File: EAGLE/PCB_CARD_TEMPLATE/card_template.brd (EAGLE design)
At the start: 24 x 60 mm, 0 parts

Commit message: have footprints complete
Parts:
- added M1: MOUNTING_3M_3.2MM, ENERTECH_MISC:MOUNTING_3M_3.2MM
- added X1: CONN_SMD_67P-P0.5-V_NASB0-S6701-TS50, ENERTECH_MISC:CONN_SMD_67P-P0.5-V_NASB0-S6701-TS50
- added X2: M.2_MKEY_FINGERS, ENERTECH_MISC:M.2_MKEY_FINGERS

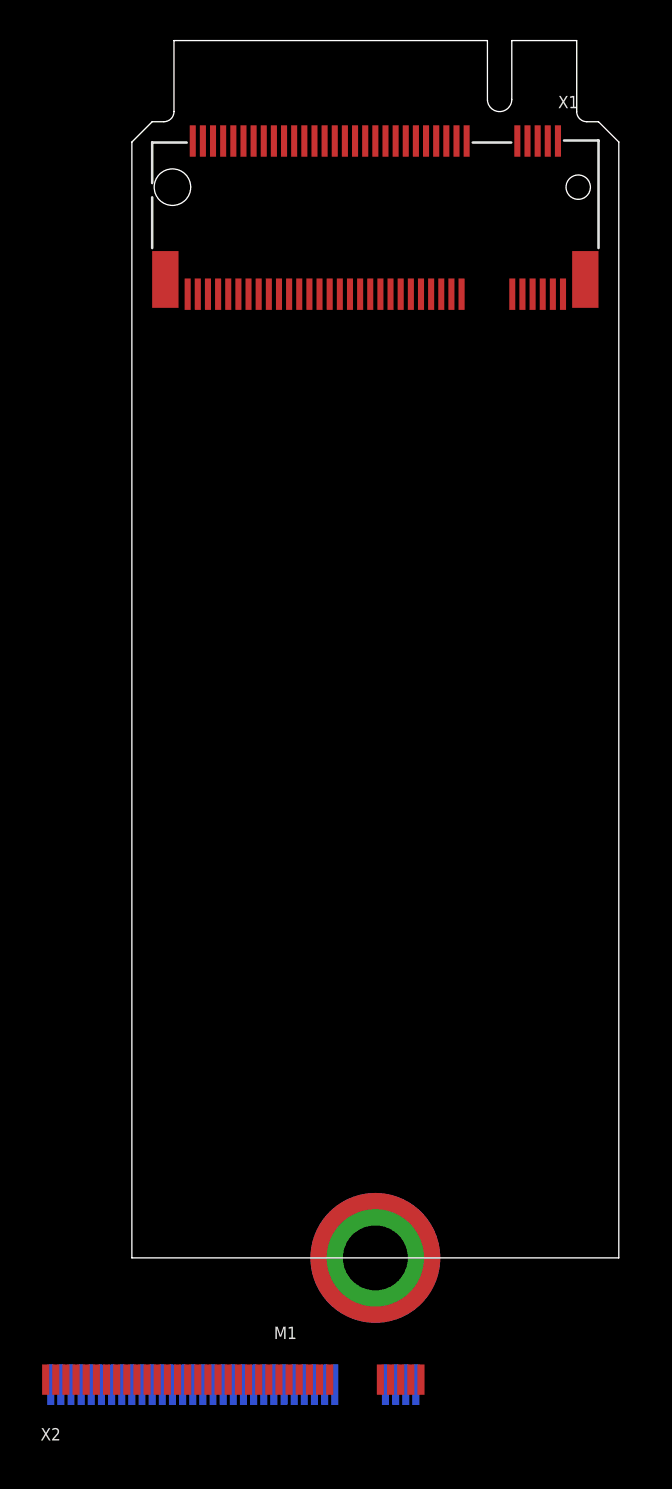
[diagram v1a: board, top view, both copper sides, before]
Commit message: completed accessory card template
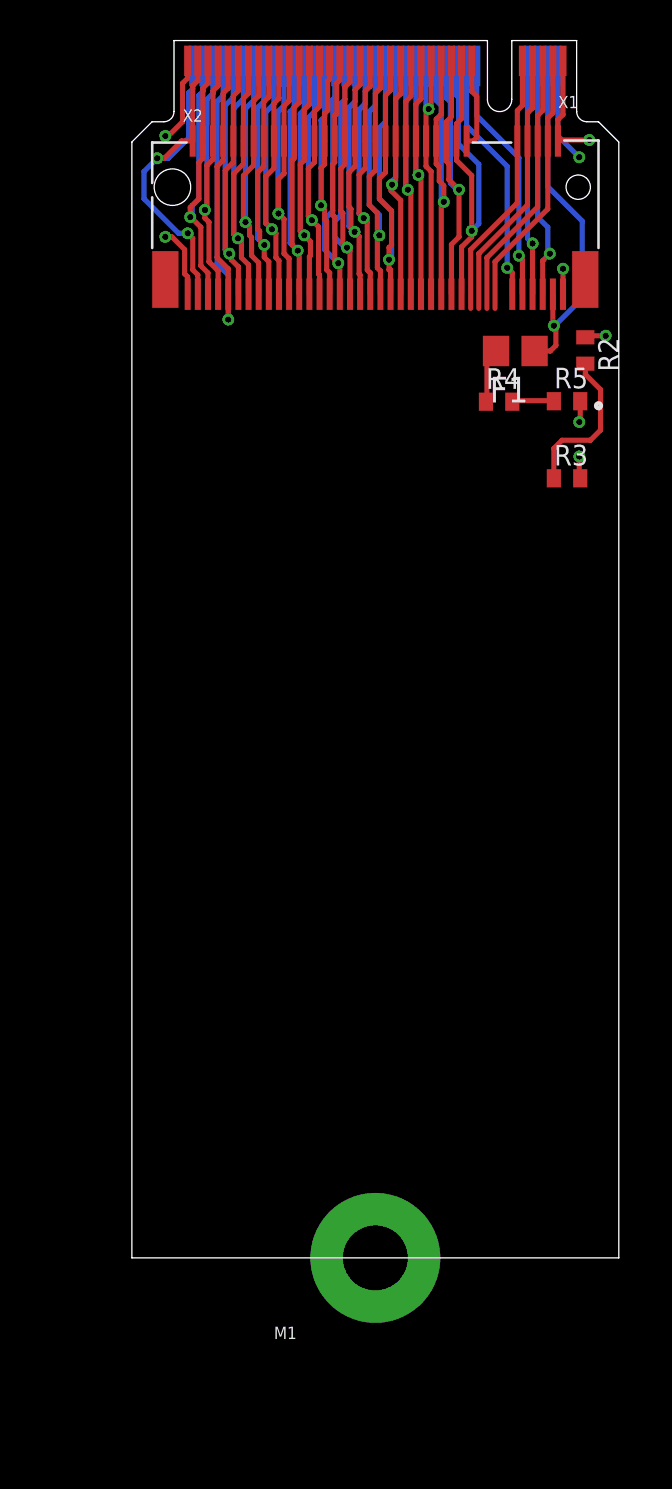
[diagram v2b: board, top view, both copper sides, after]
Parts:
- added F1: 100mA, _NIBE_rcl:R0805
- added R2, R4: 470R, _NIBE_rcl:R0603
- added R3, R5: LED_GREEN, _NIBE_rcl:R0603
- moved X2 65.4 mm to (12.0, 60.0)
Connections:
- new net +3V3: R2.1, X1.P$1, X2.74
- new net +5V: F1.2, R4.1
- new net GND: R3.2, R5.2, X1.P$2, X1.P$75, X2.1, X2.75
- new net N$1: X1.P$23, X1.P$24, X2.52, X2.53
- new net N$10: X1.P$59, X1.P$60, X2.16, X2.17
- new net N$11: X1.P$57, X1.P$58, X2.18, X2.19
- new net N$12: X1.P$55, X1.P$56, X2.20, X2.21
- new net N$13: X1.P$53, X1.P$54, X2.22, X2.23
- new net N$14: X1.P$51, X1.P$52, X2.24, X2.25
- new net N$15: X1.P$21, X1.P$22, X2.54, X2.55
- new net N$16: X1.P$27, X1.P$28, X2.48, X2.49
- new net N$17: X1.P$29, X1.P$30, X2.46, X2.47
- new net N$18: X1.P$31, X1.P$32, X2.44, X2.45
- new net N$19: X1.P$33, X1.P$34, X2.42, X2.43
- new net N$2: X1.P$25, X1.P$26, X2.50, X2.51
- new net N$20: X1.P$35, X1.P$36, X2.40, X2.41
- new net N$21: X1.P$37, X1.P$38, X2.38, X2.39
- new net N$22: X1.P$39, X1.P$40, X2.36, X2.37
- new net N$23: X1.P$41, X1.P$42, X2.34, X2.35
- new net N$24: X1.P$43, X1.P$44, X2.32, X2.33
- new net N$25: X1.P$45, X1.P$46, X2.30, X2.31
- new net N$26: X1.P$47, X1.P$48, X2.28, X2.29
- new net N$27: X1.P$49, X1.P$50, X2.26, X2.27
- new net N$28: X1.P$11, X2.56
- new net N$29: X1.P$9, X2.58
- new net N$3: X1.P$73, X1.P$74, X2.2, X2.3
- new net N$30: X1.P$7, X2.68
- new net N$31: X1.P$5, X2.70
- new net N$32: F1.1, X1.P$3, X2.72
- new net N$33: R2.2, R3.1
- new net N$35: X1.P$4, X2.73
- new net N$36: X1.P$6, X2.71
- new net N$37: X1.P$8, X2.69
- new net N$38: X1.P$10, X2.67
- new net N$39: X1.P$20, X2.57
- new net N$4: X1.P$71, X1.P$72, X2.4, X2.5
- new net N$40: R4.2, R5.1
- new net N$5: X1.P$69, X1.P$70, X2.6, X2.7
- new net N$6: X1.P$67, X1.P$68, X2.8, X2.9
- new net N$7: X1.P$65, X1.P$66, X2.10, X2.11
- new net N$8: X1.P$63, X1.P$64, X2.12, X2.13
- new net N$9: X1.P$61, X1.P$62, X2.14, X2.15
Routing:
- net N$6: track 0.00 -> 26.1 mm, vias 0 -> 1
- net N$20: track 0.00 -> 22.1 mm, vias 0 -> 1
- net N$25: track 0.00 -> 22.0 mm, vias 0 -> 1
- net N$7: track 0.00 -> 21.5 mm, vias 0 -> 1
- net N$24: track 0.00 -> 21.3 mm, vias 0 -> 1
- net N$13: track 0.00 -> 21.1 mm, vias 0 -> 1
- net N$10: track 0.00 -> 21.0 mm, vias 0 -> 1
- net N$8: track 0.00 -> 20.9 mm, vias 0 -> 1
- net N$15: track 0.00 -> 20.8 mm, vias 0 -> 1
- net N$21: track 0.00 -> 20.7 mm, vias 0 -> 1
- net N$14: track 0.00 -> 20.4 mm, vias 0 -> 1
- net N$11: track 0.00 -> 20.4 mm, vias 0 -> 1
- net N$23: track 0.00 -> 20.4 mm, vias 0 -> 1
- net N$3: track 0.00 -> 20.1 mm, vias 0 -> 2
- net N$9: track 0.00 -> 20.0 mm, vias 0 -> 1
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- added copper zone on layer 2, net +3V3
- added copper zone on layer 15, net GND

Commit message: pic24 card is done, gerbers and jlc files generated
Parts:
- removed F1: 100mA, _NIBE_rcl:R0805
- removed R4: 470R, _NIBE_rcl:R0603
- removed R5: LED_GREEN, _NIBE_rcl:R0603
- moved R3 3.00 mm to (21.4, 41.4)
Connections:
- removed net N$32: F1.1, X1.P$3, X2.72
- removed net N$35: X1.P$4, X2.73
- removed net N$40: R4.2, R5.1
- net +5V: now also X1.P$3, X2.72; no longer F1.2, R4.1
- net GND: now also X1.P$4, X2.73; no longer R5.2
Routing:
- net N$32: track 17.9 -> 0.00 mm, vias 1 -> 0
- net N$35: track 13.4 -> 0.00 mm
- net +5V: track 2.71 -> 15.7 mm, vias 0 -> 1
- net GND: track 15.5 -> 8.77 mm, vias 5 -> 4
- net N$33: track 7.73 -> 3.70 mm
- net N$40: track 2.11 -> 0.00 mm
- added copper zone on layer 1, net GND
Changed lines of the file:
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@@
 <attribute name="VALUE" x="2.5" y="54.25" locked="yes" size="0.6096" layer="27" font="vector" ratio="14"/>
-</element>
-<element name="F1" library="_NIBE_rcl" package="R0805" value="100mA" x="18.9" y="44.7" smashed="yes" rot="R180">
-<attribute name="NAME" x="19.535" y="43.43" size="1.27" layer="25" rot="R180"/>
-<attribute name="VALUE" x="19.535" y="47.24" size="1.27" layer="27" rot="R180"/>
 </element>
 <element name="R2" library="_NIBE_rcl" package="R0603" value="470R" x="22.35" y="44.725" smashed="yes" rot="R270">
@@
 <attribute name="VALUE" x="20.445" y="45.36" size="1.016" layer="27" rot="R270"/>
 </element>
-<element name="R3" library="_NIBE_rcl" package="R0603" value="LED_GREEN" x="21.45" y="38.425" smashed="yes">
-<attribute name="NAME" x="20.815" y="39.06" size="1.016" layer="25"/>
-<attribute name="VALUE" x="20.815" y="36.52" size="1.016" layer="27"/>
-</element>
-<element name="R4" library="_NIBE_rcl" package="R0603" value="470R" x="18.1" y="42.2" smashed="yes">
-<attribute name="NAME" x="17.465" y="42.835" size="1.016" layer="25"/>
-<attribute name="VALUE" x="17.465" y="40.295" size="1.016" layer="27"/>
-</element>
-<element name="R5" library="_NIBE_rcl" package="R0603" value="LED_GREEN" x="21.45" y="42.225" smashed="yes">
-<attribute name="NAME" x="20.815" y="42.86" size="1.016" layer="25"/>
-<attribute name="VALUE" x="20.815" y="40.32" size="1.016" layer="27"/>
+<element name="R3" library="_NIBE_rcl" package="R0603" value="LED_GREEN" x="21.45" y="41.425" smashed="yes">
+<attribute name="NAME" x="20.815" y="42.06" size="1.016" layer="25"/>
+<attribute name="VALUE" x="20.815" y="39.52" size="1.016" layer="27"/>
 </element>
 </elements>
@@
 <contactref element="X2" pad="75"/>
 <contactref element="R3" pad="2"/>
-<contactref element="R5" pad="2"/>
 <polygon width="0.254" layer="15" thermals="no">
 <vertex x="-1" y="-1"/>
@@
 </polygon>
 <via x="1.65" y="50.325" extent="1-16" drill="0.3"/>
-<via x="22.05" y="39.5" extent="1-16" drill="0.3"/>
-<via x="22.05" y="41.2" extent="1-16" drill="0.3"/>
-<wire x1="22.1" y1="42.225" x2="22.1" y2="41.25" width="0.254" layer="1"/>
-<wire x1="22.1" y1="41.25" x2="22.05" y2="41.2" width="0.254" layer="1"/>
-<wire x1="22.1" y1="38.425" x2="22.05" y2="38.475" width="0.254" layer="1"/>
-<wire x1="22.05" y1="38.475" x2="22.05" y2="39.5" width="0.254" layer="1"/>
-<via x="22.55" y="55.1" extent="1-16" drill="0.3"/>
-<wire x1="21" y1="55.049884375" x2="21.050115625" y2="55.1" width="0.254" layer="1"/>
-<wire x1="21.050115625" y1="55.1" x2="22.55" y2="55.1" width="0.254" layer="1"/>
-<wire x1="21.25" y1="56.35" x2="21.25" y2="59" width="0.254" layer="1"/>
-<wire x1="21" y1="55.049884375" x2="21" y2="56.1" width="0.254" layer="1"/>
-<wire x1="21" y1="56.1" x2="21.25" y2="56.35" width="0.254" layer="1"/>
+<via x="23.15" y="41.4" extent="1-16" drill="0.3"/>
+<wire x1="23.15" y1="41.4" x2="22.125" y2="41.4" width="0.254" layer="1"/>
+<wire x1="22.1" y1="41.425" x2="22.125" y2="41.4" width="0.254" layer="1"/>
+<via x="22.55" y="55.1" extent="1-16" drill="0.35"/>
 <wire x1="2.75" y1="59" x2="2.75" y2="58.15" width="0.254" layer="1"/>
 <wire x1="2.75" y1="58.15" x2="2.5" y2="57.9" width="0.254" layer="1"/>
@@
 <wire x1="2.6" y1="49.7" x2="1.975" y2="50.325" width="0.254" layer="1"/>
 <wire x1="1.975" y1="50.325" x2="1.65" y2="50.325" width="0.254" layer="1"/>
+<contactref element="X1" pad="P$4"/>
+<contactref element="X2" pad="73"/>
+<polygon width="0.1524" layer="1" thermals="no">
+<vertex x="20.3" y="54.2"/>
+<vertex x="20.3" y="55.8"/>
+<vertex x="20.6" y="56.1"/>
+<vertex x="20.6" y="59.8"/>
+<vertex x="21.5" y="59.8"/>
+<vertex x="21.5" y="56.1"/>
+<vertex x="21.9" y="55.7"/>
+<vertex x="23" y="55.7"/>
+<vertex x="23" y="54.6"/>
+<vertex x="21.5" y="54.6"/>
+<vertex x="21.1" y="54.2"/>
+</polygon>
+<wire x1="20.75" y1="59" x2="21.25" y2="59" width="0" layer="19" extent="1-1"/>
+<wire x1="21" y1="55.049884375" x2="21.25" y2="59" width="0" layer="19" extent="1-1"/>
+<wire x1="20.5" y1="55.049884375" x2="21" y2="55.049884375" width="0" layer="19" extent="1-1"/>
+<wire x1="22.55" y1="55.1" x2="21" y2="55.049884375" width="0" layer="19" extent="1-1"/>
+<wire x1="22.125" y1="41.4" x2="21" y2="55.049884375" width="0" layer="19" extent="1-1"/>
+<wire x1="2.75" y1="59" x2="20.75" y2="59" width="0" layer="19" extent="1-1"/>
+<wire x1="1.65" y1="50.325" x2="1.65" y2="55.3" width="0" layer="19" extent="1-1"/>
 </signal>
 <signal name="N$3">
@@
 <wire x1="20.5" y1="50.8" x2="20.5" y2="49.6" width="0.254" layer="16"/>
 </signal>
-<signal name="N$32">
-<contactref element="X1" pad="P$3"/>
-<contactref element="X2" pad="72"/>
-<contactref element="F1" pad="1"/>
-<wire x1="20.8" y1="45.95" x2="20.9" y2="45.85" width="0.254" layer="1"/>
-<wire x1="20.9" y1="45.85" x2="20.9" y2="44.975" width="0.254" layer="1"/>
-<wire x1="20.9" y1="44.975" x2="20.625" y2="44.7" width="0.254" layer="1"/>
-<wire x1="19.85" y1="44.7" x2="20.625" y2="44.7" width="0.254" layer="1"/>
-<wire x1="20.75" y1="47.499971875" x2="20.75" y2="46" width="0.254" layer="1"/>
-<wire x1="20.8" y1="45.95" x2="20.75" y2="46" width="0.254" layer="1"/>
-<via x="20.8" y="45.95" extent="1-16" drill="0.3"/>
-<wire x1="20.5" y1="52.8" x2="22.2" y2="51.1" width="0.254" layer="16"/>
-<wire x1="20.85" y1="45.95" x2="20.8" y2="45.95" width="0.254" layer="16"/>
-<wire x1="22.2" y1="51.1" x2="22.2" y2="47.3" width="0.254" layer="16"/>
-<wire x1="22.2" y1="47.3" x2="20.85" y2="45.95" width="0.254" layer="16"/>
-<wire x1="20.5" y1="52.8" x2="20.5" y2="58.75" width="0.254" layer="16"/>
-</signal>
-<signal name="N$35">
-<contactref element="X1" pad="P$4"/>
-<contactref element="X2" pad="73"/>
-<wire x1="20.75" y1="56.425" x2="20.75" y2="59" width="0.254" layer="1"/>
-<wire x1="20.5" y1="56.175" x2="20.75" y2="56.425" width="0.254" layer="1"/>
-<wire x1="20.5" y1="55.049884375" x2="20.5" y2="56.175" width="0.254" layer="1"/>
-<wire x1="20.5" y1="55.049884375" x2="20.5" y2="51.7" width="0.254" layer="1"/>
-<wire x1="20.5" y1="51.7" x2="17.9" y2="49.1" width="0.254" layer="1"/>
-<wire x1="17.9" y1="49.1" x2="17.9" y2="46.8" width="0.254" layer="1"/>
-</signal>
 <signal name="N$36">
 <contactref element="X1" pad="P$6"/>
@@
 <wire x1="22.35" y1="45.375" x2="22.425" y2="45.45" width="0.254" layer="1"/>
 <wire x1="22.425" y1="45.45" x2="23.35" y2="45.45" width="0.254" layer="1"/>
-<via x="22.05" y="54.25" extent="1-16" drill="0.3"/>
-<wire x1="21" y1="58.75" x2="21" y2="55.3" width="0.254" layer="16"/>
-<wire x1="22.05" y1="54.25" x2="21" y2="55.3" width="0.254" layer="16"/>
+<via x="21.95" y="54.25" extent="1-16" drill="0.35"/>
+<wire x1="21" y1="58.75" x2="21" y2="55.2" width="0.254" layer="16"/>
+<wire x1="21.95" y1="54.25" x2="21" y2="55.2" width="0.254" layer="16"/>
 </signal>
 <signal name="+5V">
-<contactref element="F1" pad="2"/>
-<contactref element="R4" pad="1"/>
-<wire x1="17.5" y1="44.25" x2="17.5" y2="42.25" width="0.254" layer="1"/>
-<wire x1="17.95" y1="44.7" x2="17.5" y2="44.25" width="0.254" layer="1"/>
-<wire x1="17.5" y1="42.25" x2="17.45" y2="42.2" width="0.254" layer="1"/>
+<contactref element="X1" pad="P$3"/>
+<contactref element="X2" pad="72"/>
+<wire x1="20.75" y1="47.499971875" x2="20.75" y2="46" width="0.254" layer="1"/>
+<wire x1="20.8" y1="45.95" x2="20.75" y2="46" width="0.254" layer="1"/>
+<via x="20.8" y="45.95" extent="1-16" drill="0.3"/>
+<wire x1="20.5" y1="52.8" x2="22.2" y2="51.1" width="0.254" layer="16"/>
+<wire x1="20.85" y1="45.95" x2="20.8" y2="45.95" width="0.254" layer="16"/>
+<wire x1="22.2" y1="51.1" x2="22.2" y2="47.3" width="0.254" layer="16"/>
+<wire x1="22.2" y1="47.3" x2="20.85" y2="45.95" width="0.254" layer="16"/>
+<wire x1="20.5" y1="52.8" x2="20.5" y2="58.75" width="0.254" layer="16"/>
 </signal>
 <signal name="N$33">
 <contactref element="R2" pad="2"/>
 <contactref element="R3" pad="1"/>
-<wire x1="20.8" y1="38.425" x2="20.8" y2="39.9" width="0.254" layer="1"/>
-<wire x1="22.35" y1="43.55" x2="22.35" y2="44.075" width="0.254" layer="1"/>
-<wire x1="20.8" y1="39.9" x2="21.2" y2="40.3" width="0.254" layer="1"/>
-<wire x1="21.2" y1="40.3" x2="22.6" y2="40.3" width="0.254" layer="1"/>
-<wire x1="22.6" y1="40.3" x2="23.1" y2="40.8" width="0.254" layer="1"/>
-<wire x1="23.1" y1="40.8" x2="23.1" y2="42.8" width="0.254" layer="1"/>
-<wire x1="23.1" y1="42.8" x2="22.35" y2="43.55" width="0.254" layer="1"/>
-</signal>
-<signal name="N$40">
-<contactref element="R5" pad="1"/>
-<contactref element="R4" pad="2"/>
-<wire x1="20.75" y1="42.25" x2="18.75" y2="42.25" width="0.254" layer="1"/>
-<wire x1="18.75" y1="42.25" x2="18.75" y2="42.2" width="0.254" layer="1"/>
-<wire x1="20.75" y1="42.25" x2="20.8" y2="42.225" width="0.254" layer="1"/>
+<wire x1="22.35" y1="44.075" x2="22.35" y2="43.25" width="0.254" layer="1"/>
+<wire x1="21.9" y1="42.8" x2="21.2" y2="42.8" width="0.254" layer="1"/>
+<wire x1="21.2" y1="42.8" x2="20.8" y2="42.4" width="0.254" layer="1"/>
+<wire x1="20.8" y1="42.4" x2="20.8" y2="41.425" width="0.254" layer="1"/>
+<wire x1="22.35" y1="43.25" x2="21.9" y2="42.8" width="0.254" layer="1"/>
 </signal>
 </signals>
